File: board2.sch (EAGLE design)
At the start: 76 parts, among them Q1 7.68M, Q2 16MHz

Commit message: Added RX-TX pin jumpers. IMPORTANT: changed the 5V&GND of ICSP connector to the isolated side (after iso)
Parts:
- added RX-TX: (no value), SparkFun-Connectors:M02PTH
- Q1: value 7.68M -> 7.68MHz
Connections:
- new net RX: ATMEGA328.PD0(RXD), RX-TX.1
- new net TX: ATMEGA328.PD1(TXD), RX-TX.2
- net 5V: no longer ICSP.2
- net 5V_ISO: now also ICSP.2
- net GND: no longer ICSP.6
- net GND_ISO: now also ICSP.6
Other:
- note added: "Measuring PCB v2.3"
- note removed: "Measuring PCB v2.2"
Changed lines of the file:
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@@
 <part name="C6" library="adafruit" deviceset="C-US" device="C3216" value="10u"/>
 <part name="C7" library="adafruit" deviceset="C-US" device="C3216" value="0.1u"/>
-<part name="Q1" library="adafruit" deviceset="CRYSTAL" device="HC49U-V" value="7.68M"/>
+<part name="Q1" library="adafruit" deviceset="CRYSTAL" device="HC49U-V" value="7.68MHz"/>
 <part name="C8" library="adafruit" deviceset="C-US" device="C3216" value="18p"/>
 <part name="C9" library="adafruit" deviceset="C-US" device="C3216" value="18p"/>
@@
 <part name="NON-ISOLATED_CON" library="adafruit" deviceset="PINHD-2X4" device=""/>
 <part name="1WIRE-BUS" library="Paschalis_connectors" deviceset="PHOENIX-TERMINAL-3PIN" device=""/>
+<part name="RX-TX" library="SparkFun-Connectors" deviceset="M02" device="PTH"/>
 </parts>
 <sheets>
@@
 <text x="-5.08" y="-175.26" size="5.08" layer="98">Standalone Arduino (atmega328)</text>
 <text x="327.66" y="-175.26" size="5.08" layer="98">Connectors</text>
-<text x="406.4" y="-228.6" size="6.4516" layer="98">Measuring PCB v2.2</text>
+<text x="406.4" y="-228.6" size="6.4516" layer="98">Measuring PCB v2.3</text>
 <wire x1="370.84" y1="-281.94" x2="370.84" y2="-248.92" width="0.1524" layer="98"/>
 <wire x1="370.84" y1="-248.92" x2="370.84" y2="-233.68" width="0.1524" layer="98"/>
@@
 <instance part="NON-ISOLATED_CON" gate="A" x="467.36" y="-203.2"/>
 <instance part="1WIRE-BUS" gate="G$1" x="365.76" y="-193.04"/>
+<instance part="RX-TX" gate="G$1" x="353.06" y="-215.9" rot="R180"/>
 </instances>
 <busses>
@@
 <label x="58.42" y="-25.4" size="1.778" layer="95" xref="yes"/>
 <pinref part="F1" gate="G$1" pin="2B"/>
-<wire x1="33.02" y1="-35.56" x2="30.48" y2="-35.56" width="0.1524" layer="91"/>
+<wire x1="30.48" y1="-35.56" x2="33.02" y2="-35.56" width="0.1524" layer="91"/>
+<junction x="33.02" y="-35.56"/>
 </segment>
 <segment>
@@
 <label x="15.24" y="2.54" size="1.778" layer="95" rot="R180" xref="yes"/>
 <pinref part="F1" gate="G$1" pin="1B"/>
-<wire x1="22.86" y1="-35.56" x2="25.4" y2="-35.56" width="0.1524" layer="91"/>
+<wire x1="25.4" y1="-35.56" x2="22.86" y2="-35.56" width="0.1524" layer="91"/>
+<junction x="22.86" y="-35.56"/>
 </segment>
 </net>
@@
 <wire x1="370.84" y1="-38.1" x2="370.84" y2="-35.56" width="0.1524" layer="91"/>
 <junction x="370.84" y="-35.56"/>
-</segment>
-<segment>
-<pinref part="ICSP" gate="G$1" pin="2"/>
-<wire x1="419.1" y1="-185.42" x2="421.64" y2="-185.42" width="0.1524" layer="91"/>
-<label x="421.64" y="-185.42" size="1.778" layer="95" xref="yes"/>
 </segment>
 </net>
@@
 <junction x="350.52" y="-53.34"/>
 <label x="342.9" y="-53.34" size="1.778" layer="95" rot="R180" xref="yes"/>
-</segment>
-<segment>
-<pinref part="ICSP" gate="G$1" pin="6"/>
-<wire x1="419.1" y1="-190.5" x2="421.64" y2="-190.5" width="0.1524" layer="91"/>
-<label x="421.64" y="-190.5" size="1.778" layer="95" xref="yes"/>
 </segment>
 </net>
@@
 <wire x1="464.82" y1="-198.12" x2="447.04" y2="-198.12" width="0.1524" layer="91"/>
 <label x="447.04" y="-198.12" size="1.778" layer="95" rot="R180" xref="yes"/>
+</segment>
+<segment>
+<pinref part="ICSP" gate="G$1" pin="2"/>
+<wire x1="419.1" y1="-185.42" x2="421.64" y2="-185.42" width="0.1524" layer="91"/>
+<label x="421.64" y="-185.42" size="1.778" layer="95" xref="yes"/>
 </segment>
 </net>
@@
 <label x="480.06" y="-198.12" size="1.778" layer="95" xref="yes"/>
 </segment>
+<segment>
+<pinref part="ICSP" gate="G$1" pin="6"/>
+<wire x1="419.1" y1="-190.5" x2="421.64" y2="-190.5" width="0.1524" layer="91"/>
+<label x="421.64" y="-190.5" size="1.778" layer="95" xref="yes"/>
+</segment>
 </net>
 <net name="IN2_ISO" class="0">
@@
 <segment>
 <pinref part="ICSP" gate="G$1" pin="4"/>
-<wire x1="419.1" y1="-187.96" x2="429.26" y2="-187.96" width="0.1524" layer="91"/>
-<label x="429.26" y="-187.96" size="1.778" layer="95" xref="yes"/>
+<wire x1="419.1" y1="-187.96" x2="434.34" y2="-187.96" width="0.1524" layer="91"/>
+<label x="434.34" y="-187.96" size="1.778" layer="95" xref="yes"/>
 </segment>
 </net>
@@
 </segment>
 </net>
+<net name="RX" class="0">
+<segment>
+<pinref part="ATMEGA328" gate="U$1" pin="PD0(RXD)"/>
+<wire x1="210.82" y1="-231.14" x2="215.9" y2="-231.14" width="0.1524" layer="91"/>
+<label x="215.9" y="-231.14" size="1.778" layer="95" xref="yes"/>
+</segment>
+<segment>
+<pinref part="RX-TX" gate="G$1" pin="1"/>
+<wire x1="345.44" y1="-215.9" x2="337.82" y2="-215.9" width="0.1524" layer="91"/>
+<label x="337.82" y="-215.9" size="1.778" layer="95" rot="R180" xref="yes"/>
+</segment>
+</net>
+<net name="TX" class="0">
+<segment>
+<pinref part="ATMEGA328" gate="U$1" pin="PD1(TXD)"/>
+<wire x1="210.82" y1="-233.68" x2="228.6" y2="-233.68" width="0.1524" layer="91"/>
+<label x="228.6" y="-233.68" size="1.778" layer="95" xref="yes"/>
+</segment>
+<segment>
+<pinref part="RX-TX" gate="G$1" pin="2"/>
+<wire x1="345.44" y1="-218.44" x2="342.9" y2="-218.44" width="0.1524" layer="91"/>
+<label x="342.9" y="-218.44" size="1.778" layer="95" rot="R180" xref="yes"/>
+</segment>
+</net>

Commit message: Added RX,TX header, D0-3 pinout. Changed the polygon shape (radius in corners). Created first try in 3D for Inventor.
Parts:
- added D0-D3: (no value), SparkFun-Connectors:M04NO_SILK_ALL_ROUND
- AIN6-7: device SparkFun-Connectors:M02PTH -> SparkFun-Connectors:M021X02_NO_SILK
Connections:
- removed net N$18: ADS1256.AIN6, AIN6-7.2
- removed net N$19: ADS1256.AIN7, AIN6-7.1
- new net AIN6: ADS1256.AIN6, AIN6-7.1
- new net AIN7: ADS1256.AIN7, AIN6-7.2
- new net D0: ADS1256.D0/CLKOUT, D0-D3.1
- new net D1: ADS1256.D1, D0-D3.2
- new net D2: ADS1256.D2, D0-D3.3
- new net D3: ADS1256.D3, D0-D3.4
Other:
- note added: "IMEC KU Leuven"
- note added: "This board measures Voltage, Current and Temperature of a PV panel.In addition, it gets Date and Time stamp. The data are collected by the microprocessor Atmega328 and send out as I2C packages to master board. Every connection outside the board is isolated. (NOMINAL 40V@8A, MAX 44V@15A)"
- note removed: "This board measures Voltage, Current and Temperature of a PV panel.In addition, it gets Date and Time stamp. The data are collected by the microprocessor Atmega328 and send out as I2C packages to master board. Every connection outside the board is isolated. (NOMINAL 40V@8A, MAX 45V@15A)"
- moved on the sheet: ADS1256, AIN6-7, ATMEGA328, BAT1, C1, C2, C28, C29, C30, C31, C32, C33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

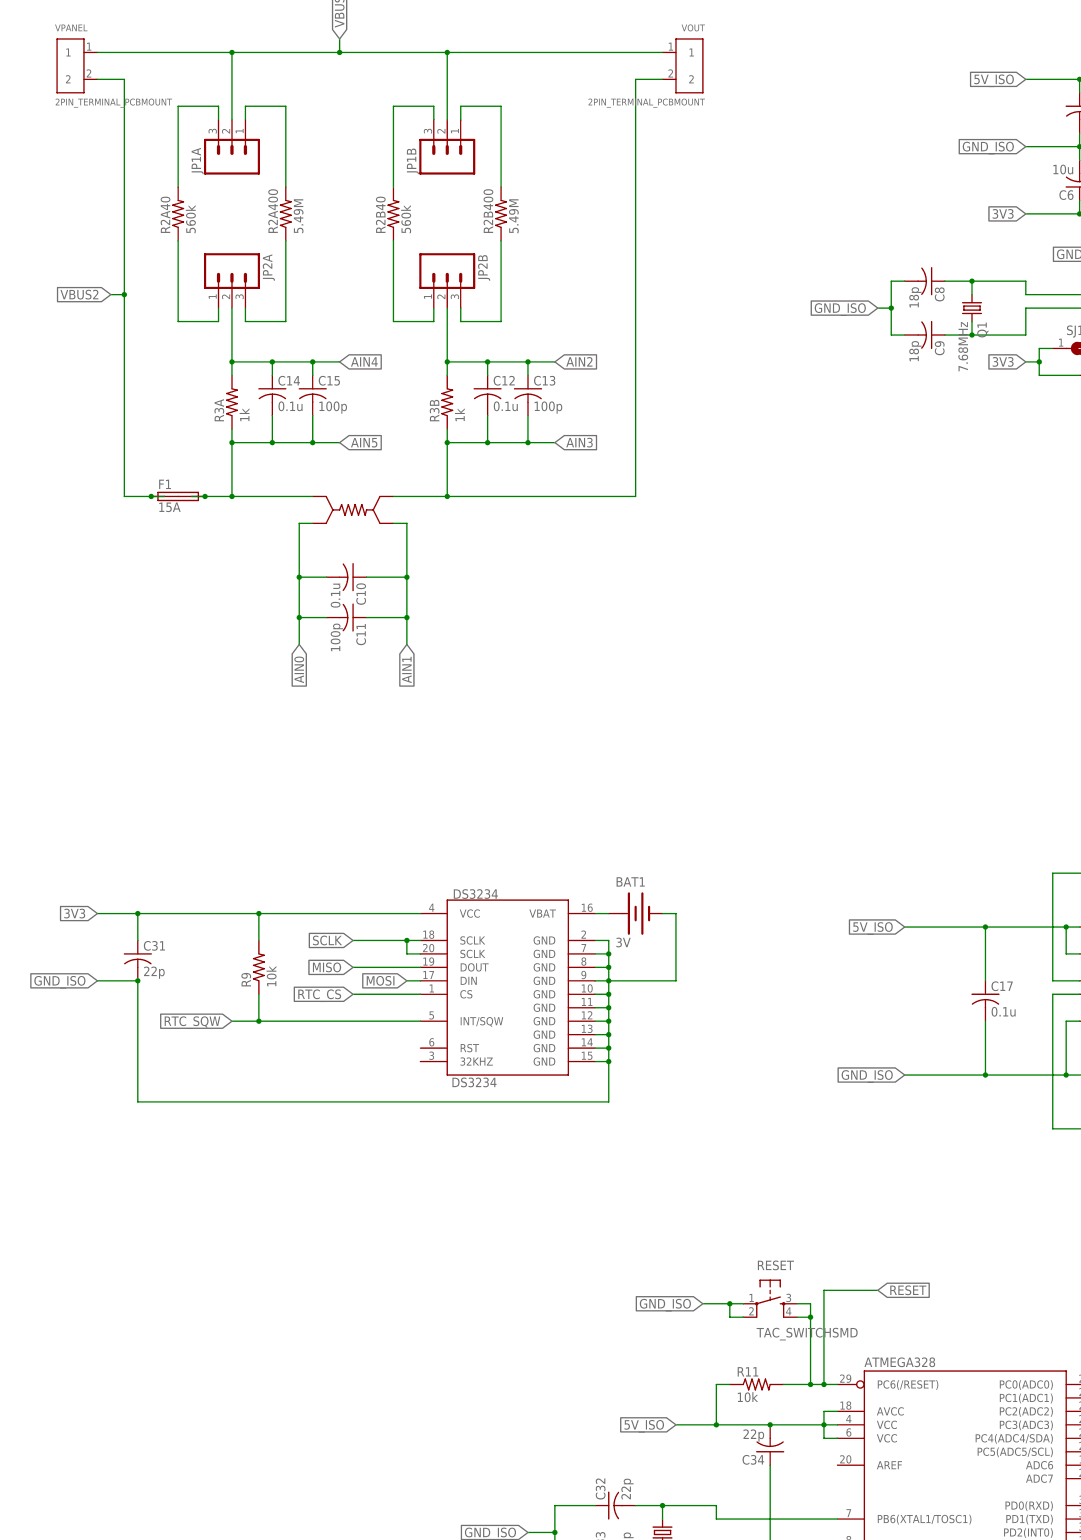
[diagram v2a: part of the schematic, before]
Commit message: Footprints updated and small changes
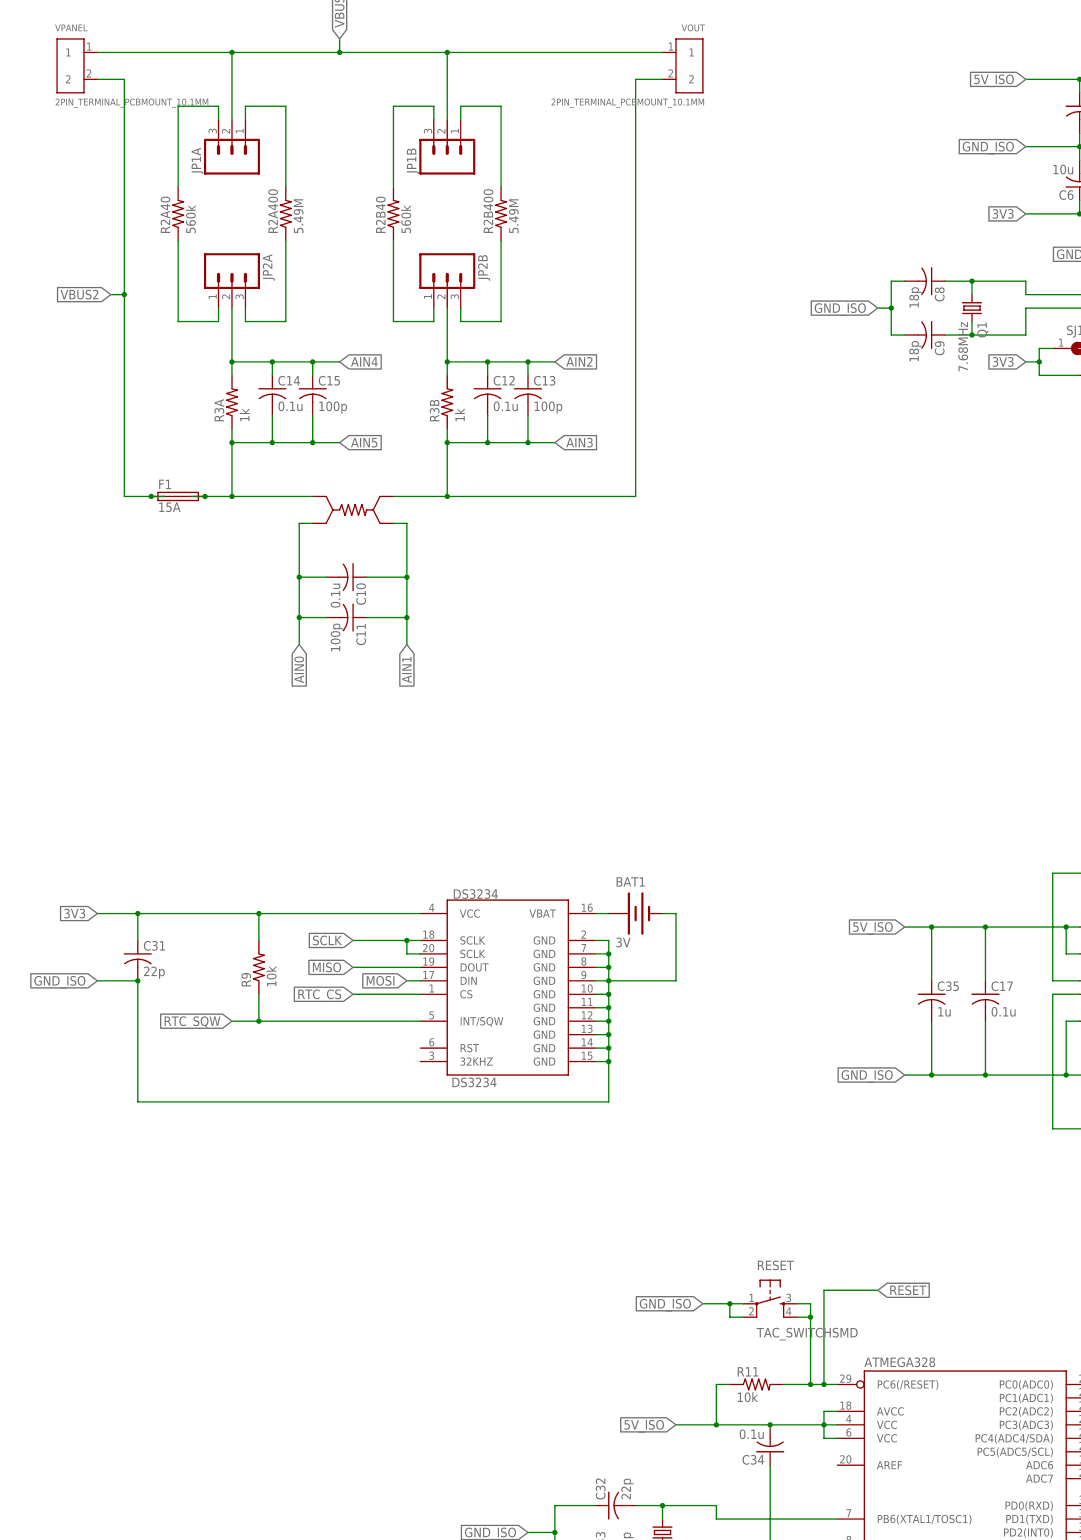
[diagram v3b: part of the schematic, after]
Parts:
- added C35: 1u, adafruit:C-USC3216
- C34: value 22p -> 0.1u
- VOUT, VPANEL: value 2PIN_TERMINAL_PCBMOUNT -> 2PIN_TERMINAL_PCBMOUNT_10.1MM; device TE CONNECTIVITY:2PIN_TERMINAL_PCBMOUNT -> TE CONNECTIVITY:2PIN_TERMINAL_PCBMOUNT_10.1MM
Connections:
- net 5V_ISO: now also C35.1
- net GND_ISO: now also C35.2
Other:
- note added: "Measuring PCB v2.4"
- note removed: "Measuring PCB v2.3"
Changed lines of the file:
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@@
 </classes>
 <parts>
-<part name="VPANEL" library="TE CONNECTIVITY" deviceset="2PIN_TERMINAL_PCBMOUNT" device=""/>
-<part name="VOUT" library="TE CONNECTIVITY" deviceset="2PIN_TERMINAL_PCBMOUNT" device=""/>
+<part name="VPANEL" library="TE CONNECTIVITY" deviceset="2PIN_TERMINAL_PCBMOUNT_10.1MM" device=""/>
+<part name="VOUT" library="TE CONNECTIVITY" deviceset="2PIN_TERMINAL_PCBMOUNT_10.1MM" device=""/>
 <part name="JP1A" library="SparkFun-Connectors" deviceset="M03" device="PTH"/>
 <part name="JP1B" library="SparkFun-Connectors" deviceset="M03" device="PTH"/>
@@
 <part name="C33" library="adafruit" deviceset="C-US" device="C3216" value="22p"/>
 <part name="Q2" library="adafruit" deviceset="CRYSTAL" device="HC49U-V" value="16MHz"/>
-<part name="C34" library="adafruit" deviceset="C-US" device="C3216" value="22p"/>
+<part name="C34" library="adafruit" deviceset="C-US" device="C3216" value="0.1u"/>
 <part name="R10" library="adafruit" deviceset="R-US_" device="R3216" value="4.7k"/>
 <part name="R11" library="adafruit" deviceset="R-US_" device="R3216" value="10k"/>
@@
 <part name="RX-TX" library="SparkFun-Connectors" deviceset="M02" device="PTH"/>
 <part name="D0-D3" library="SparkFun-Connectors" deviceset="M04" device="NO_SILK_ALL_ROUND"/>
+<part name="C35" library="adafruit" deviceset="C-US" device="C3216" value="1u"/>
 </parts>
 <sheets>
@@
 <text x="-5.08" y="-175.26" size="5.08" layer="98">Standalone Arduino (atmega328)</text>
 <text x="322.58" y="-175.26" size="5.08" layer="98">Connectors</text>
-<text x="381" y="-228.6" size="6.4516" layer="98">Measuring PCB v2.3</text>
+<text x="381" y="-228.6" size="6.4516" layer="98">Measuring PCB v2.4</text>
 <wire x1="370.84" y1="-281.94" x2="370.84" y2="-248.92" width="0.1524" layer="98"/>
 <wire x1="370.84" y1="-248.92" x2="370.84" y2="-233.68" width="0.1524" layer="98"/>
@@
 <instance part="RX-TX" gate="G$1" x="353.06" y="-215.9" rot="R180"/>
 <instance part="D0-D3" gate="G$1" x="350.52" y="-256.54" rot="R180"/>
+<instance part="C35" gate="G$1" x="170.18" y="-129.54"/>
 </instances>
 <busses>
@@
 <wire x1="198.12" y1="-116.84" x2="195.58" y2="-116.84" width="0.1524" layer="91"/>
 <wire x1="195.58" y1="-116.84" x2="180.34" y2="-116.84" width="0.1524" layer="91"/>
-<wire x1="180.34" y1="-116.84" x2="165.1" y2="-116.84" width="0.1524" layer="91"/>
+<wire x1="180.34" y1="-116.84" x2="170.18" y2="-116.84" width="0.1524" layer="91"/>
 <pinref part="C17" gate="G$1" pin="1"/>
+<wire x1="170.18" y1="-116.84" x2="165.1" y2="-116.84" width="0.1524" layer="91"/>
 <wire x1="180.34" y1="-127" x2="180.34" y2="-116.84" width="0.1524" layer="91"/>
 <junction x="180.34" y="-116.84"/>
@@
 <junction x="195.58" y="-116.84"/>
 <label x="165.1" y="-116.84" size="1.778" layer="95" rot="R180" xref="yes"/>
+<pinref part="C35" gate="G$1" pin="1"/>
+<wire x1="170.18" y1="-127" x2="170.18" y2="-116.84" width="0.1524" layer="91"/>
+<junction x="170.18" y="-116.84"/>
 </segment>
 <segment>
@@
 </segment>
 <segment>
-<wire x1="165.1" y1="-144.78" x2="180.34" y2="-144.78" width="0.1524" layer="91"/>
+<wire x1="165.1" y1="-144.78" x2="170.18" y2="-144.78" width="0.1524" layer="91"/>
+<wire x1="170.18" y1="-144.78" x2="180.34" y2="-144.78" width="0.1524" layer="91"/>
 <wire x1="180.34" y1="-144.78" x2="195.58" y2="-144.78" width="0.1524" layer="91"/>
 <pinref part="C17" gate="G$1" pin="2"/>
@@
 <junction x="261.62" y="-144.78"/>
 <wire x1="248.92" y1="-144.78" x2="261.62" y2="-144.78" width="0.1524" layer="91"/>
-</segment>
-<segment>
+<pinref part="C35" gate="G$1" pin="2"/>
+<wire x1="170.18" y1="-134.62" x2="170.18" y2="-144.78" width="0.1524" layer="91"/>
+<junction x="170.18" y="-144.78"/>
+</segment>
+<segment>
